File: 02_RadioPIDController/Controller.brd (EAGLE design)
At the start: 118.1 x 121.6 mm, 18 parts, among them IC1 7805TV, M1 ARDUINO-NANO-3.0, X5 236-403, X6 236-403, X7 MSTBA2

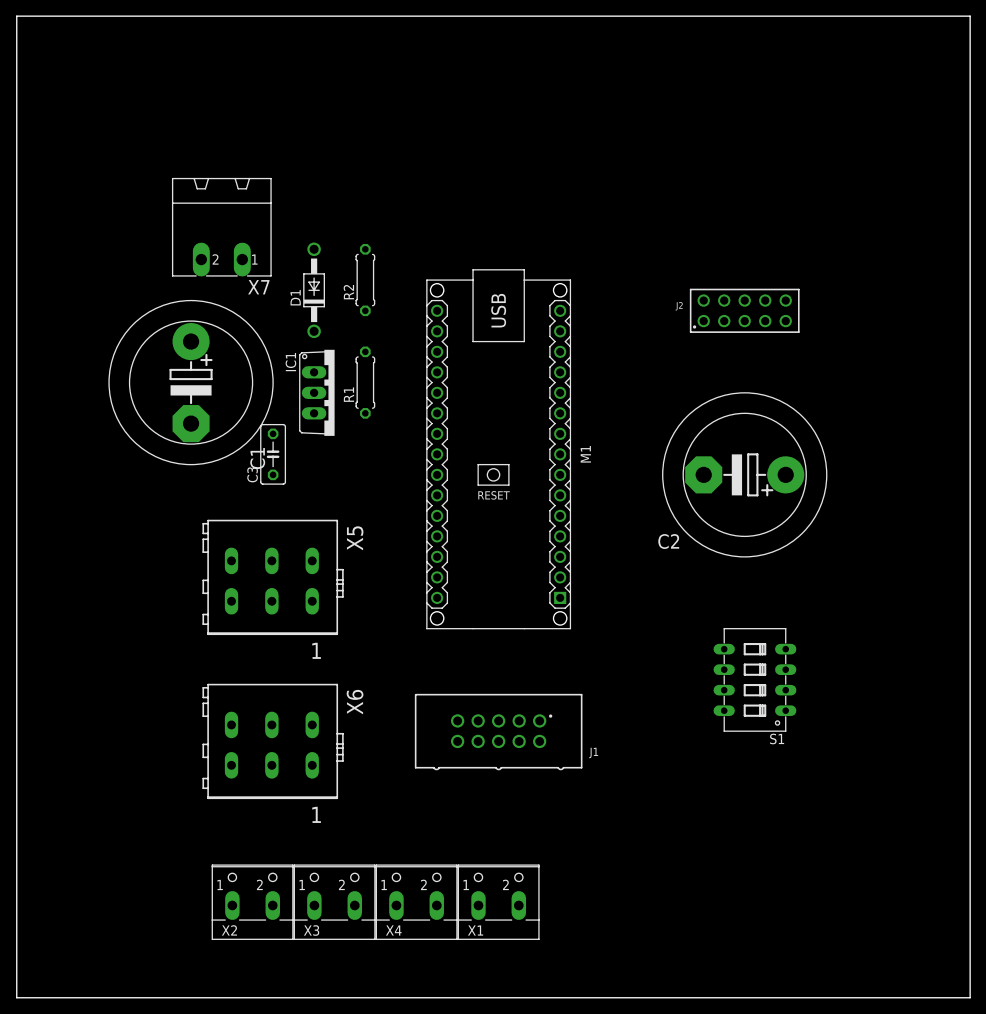
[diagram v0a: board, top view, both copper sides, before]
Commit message: Doc for radio and controller 2
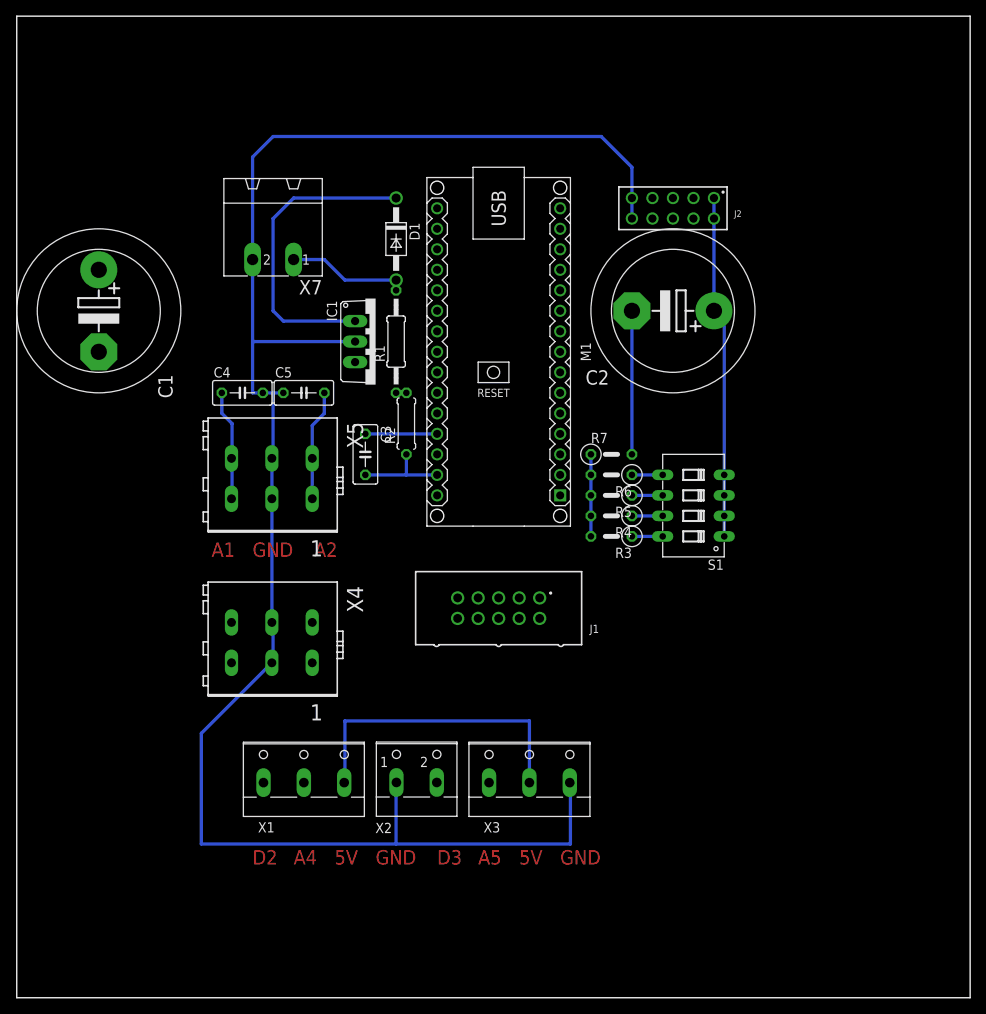
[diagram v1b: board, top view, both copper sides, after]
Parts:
- removed X6: 236-403, con-wago_236:P-236-403
- added C4, C5: 0.1u, rcl:C050-030X075
- added R3: 2.2k, resistor:0207/5V
- added R4: 4.7k, resistor:0207/5V
- added R5: 10k, resistor:0207/5V
- added R6: 20k, resistor:0207/5V
- added R7: 1.6k, resistor:0207/5V
- C1: value (none) -> Not Installed
- C2: value (none) -> 470u 25V
- C3: value (none) -> 0.1u
- R1: value (none) -> 4700; device resistor:0207/7 -> resistor:0207/12
- R2: value (none) -> 2000
- X1, X3: device con-wago-500:W237-102 -> con-wago-500:W237-103
- X4: value (none) -> Not Installed; device con-wago-500:W237-102 -> con-wago_236:P-236-403
- moved X4 36.4 mm to (31.8, 44.5), turned to 270 degrees
- moved X3 28.5 mm to (63.5, 27.9)
- moved X1 28.5 mm to (35.6, 27.9)
- moved X2 25.4 mm to (49.5, 27.9)
- moved S1 22.9 mm to (83.8, 61.0)
- moved C2 22.2 mm to (81.3, 85.1)
- moved R2 18.5 mm to (48.3, 71.1)
- moved J2 15.5 mm to (81.3, 97.8), turned to 180 degrees
- moved J1 15.2 mm to (59.7, 48.3)
- moved C1 14.5 mm to (10.2, 85.1)
- moved M1 12.7 mm to (59.7, 80.0)
- moved X5 12.7 mm to (31.8, 64.8)
- moved D1 12.0 mm to (47.0, 94.0), turned to 270 degrees
- moved C3 11.4 mm to (43.2, 67.3), turned to 270 degrees
- moved IC1 8.13 mm to (44.5, 81.3)
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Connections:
- new net N$4: R4.1, S1.7
- new net N$5: R5.1, S1.6
- new net N$6: R6.1, S1.5
- new net N$7: R3.1, S1.8
- net +5V: now also C3.1, S1.1, S1.2, S1.3, S1.4, X1.3, X3.2
- net A1: now also C4.1, X5.L3.1, X5.L3.2
- net A2: now also C5.2, X5.L1.1, X5.L1.2
- net A4: now also X1.2
- net A5: now also X3.1
- net BAT_MON: now also R1.1, R2.2; no longer R1.2, R2.1
- net D2: now also X1.1
- net D3: now also X2.2
- net DIP_SW: now also R3.2, R4.2, R5.2, R6.2, R7.1
- net GND: now also C3.2, C4.2, C5.1, R2.1, R7.2, X2.1, X3.3, X4.L2.1, X4.L2.2, X5.L2.1, X5.L2.2; no longer R1.1
- net N$1: now also R1.2; no longer R2.2
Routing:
- net GND: track 0.00 -> 253.3 mm
- net +5V: track 0.00 -> 89.5 mm
- net N$3: track 0.00 -> 38.4 mm
- net N$1: track 0.00 -> 15.0 mm
- net A2: track 0.00 -> 13.7 mm
- net A1: track 0.00 -> 13.7 mm
- net DIP_SW: track 0.00 -> 10.2 mm
- net N$7: track 0.00 -> 3.81 mm
- net N$6: track 0.00 -> 3.81 mm
- net N$5: track 0.00 -> 3.81 mm
- net N$4: track 0.00 -> 3.81 mm
- net BAT_MON: track 0.00 -> 1.27 mm
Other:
- board text added: "5V"
- board text added: "A1"
- board text added: "A2"
- board text added: "A4"
- board text added: "A5"
- board text added: "D2"
- board text added: "D3"
- board text added: "GND"
